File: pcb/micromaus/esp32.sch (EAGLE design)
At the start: 1 part, among them U1 ESP32-S2-WROOM

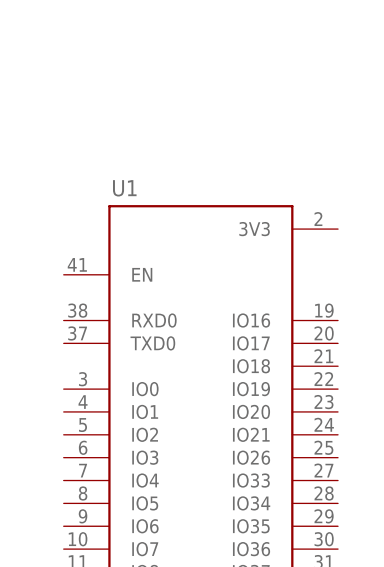
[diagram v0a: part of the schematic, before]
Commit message: added resistor
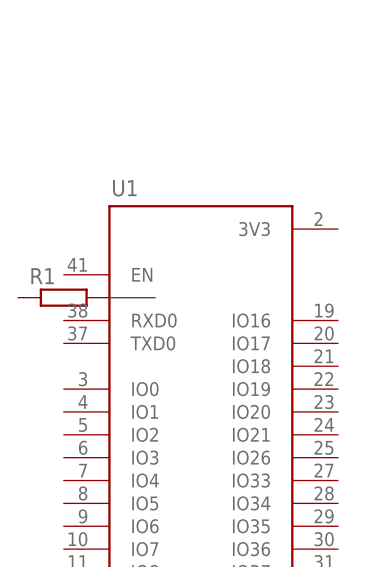
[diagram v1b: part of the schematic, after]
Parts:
- added R1: (no value), rcl:R-EU_R0603
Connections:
- new net N$1: R1.2, U1.IO0
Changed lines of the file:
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@@
 <drawing>
 <settings>
-<setting alwaysvectorfont="yes"/>
+<setting alwaysvectorfont="no"/>
 <setting verticaltext="up"/>
 </settings>
@@
 <layers>
 <layer number="1" name="Top" color="4" fill="1" visible="no" active="no"/>
+<layer number="2" name="Route2" color="1" fill="3" visible="no" active="no"/>
+<layer number="3" name="Route3" color="4" fill="3" visible="no" active="no"/>
+<layer number="4" name="Route4" color="1" fill="4" visible="no" active="no"/>
+<layer number="5" name="Route5" color="4" fill="4" visible="no" active="no"/>
+<layer number="6" name="Route6" color="1" fill="8" visible="no" active="no"/>
+<layer number="7" name="Route7" color="4" fill="8" visible="no" active="no"/>
+<layer number="8" name="Route8" color="1" fill="2" visible="no" active="no"/>
+<layer number="9" name="Route9" color="4" fill="2" visible="no" active="no"/>
+<layer number="10" name="Route10" color="1" fill="7" visible="no" active="no"/>
+<layer number="11" name="Route11" color="4" fill="7" visible="no" active="no"/>
+<layer number="12" name="Route12" color="1" fill="5" visible="no" active="no"/>
+<layer number="13" name="Route13" color="4" fill="5" visible="no" active="no"/>
+<layer number="14" name="Route14" color="1" fill="6" visible="no" active="no"/>
+<layer number="15" name="Route15" color="4" fill="6" visible="no" active="no"/>
 <layer number="16" name="Bottom" color="1" fill="1" visible="no" active="no"/>
 <layer number="17" name="Pads" color="2" fill="1" visible="no" active="no"/>
@@
 <parts>
 <part name="U1" library="ESP32-S2-WROOM" deviceset="ESP32-S2-WROOM" device=""/>
+<part name="R1" library="rcl" library_urn="urn:adsk.eagle:library:334" deviceset="R-EU_" device="R0603" package3d_urn="urn:adsk.eagle:package:23555/3"/>
 </parts>
 <sheets>
@@
 <attribute name="VALUE" x="58.3733" y="2.4319" size="1.78345" layer="96"/>
 </instance>
+<instance part="R1" gate="G$1" x="53.34" y="60.96" smashed="yes">
+<attribute name="NAME" x="49.53" y="62.4586" size="1.778" layer="95"/>
+<attribute name="VALUE" x="49.53" y="57.658" size="1.778" layer="96"/>
+</instance>
 </instances>
 <busses>
 </busses>
 <nets>
+<net name="N$1" class="0">
+<segment>
+<pinref part="R1" gate="G$1" pin="2"/>
+<pinref part="U1" gate="G$1" pin="IO0"/>
+<wire x1="58.42" y1="60.96" x2="63.5" y2="60.96" width="0.1524" layer="91"/>
+</segment>
+</net>
 </nets>
 </sheet>
@@
 </schematic>
 </drawing>
+<compatibility>
+<note version="8.2" severity="warning">
+Since Version 8.2, EAGLE supports online libraries. The ids
+of those online libraries will not be understood (or retained)
+with this version.
+</note>
+<note version="8.3" severity="warning">
+Since Version 8.3, EAGLE supports URNs for individual library
+assets (packages, symbols, and devices). The URNs of those assets
+will not be understood (or retained) with this version.
+</note>
+<note version="8.3" severity="warning">
+Since Version 8.3, EAGLE supports the association of 3D packages
+with devices in libraries, schematics, and board files. Those 3D
+packages will not be understood (or retained) with this version.
+</note>
+<note version="8.4" severity="warning">
+Since Version 8.4, EAGLE supports properties for SPICE simulation.
+Probes in schematics and SPICE mapping objects found in parts and library devices
+will not be understood with this version. Update EAGLE to the latest version
+for full support of SPICE simulation.
+</note>
+</compatibility>
 </eagle>

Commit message: added shit
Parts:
- added IC1: EPF10K30-Q240, altera:EPF10K30-Q240

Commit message: updated libs & wip usb uart
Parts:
- added IC2: CP2102, silabs:CP2102
- added U2: CH340C, CH340C:CH340C
- added X1: MINI-USB_SHIELD5P2-32005-601, con-cypressindustries:MINI-USB_SHIELD5P2-32005-601
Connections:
- new net GND: X1G41.4, X1G41.5
- new net N$3: U2.VCC
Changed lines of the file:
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@@
 <drawing>
 <settings>
-<setting alwaysvectorfont="no"/>
+<setting alwaysvectorfont="yes"/>
 <setting verticaltext="up"/>
 </settings>
@@
 <part name="R1" library="rcl" library_urn="urn:adsk.eagle:library:334" deviceset="R-EU_" device="R0603" package3d_urn="urn:adsk.eagle:package:23555/3"/>
 <part name="IC1" library="altera" library_urn="urn:adsk.eagle:library:97" deviceset="EPF10K30-Q240" device="" package3d_urn="urn:adsk.eagle:package:8081272/1"/>
+<part name="IC2" library="silabs" library_urn="urn:adsk.eagle:library:358" deviceset="CP210*" device="" package3d_urn="urn:adsk.eagle:package:26377/1" technology="2"/>
+<part name="U2" library="CH340C" deviceset="CH340C" device=""/>
+<part name="X1" library="con-cypressindustries" library_urn="urn:adsk.eagle:library:138" deviceset="MINI-USB_SHIELD5P2-" device="32005-601" package3d_urn="urn:adsk.eagle:package:6465/1"/>
+<part name="SUPPLY1" library="supply2" library_urn="urn:adsk.eagle:library:372" deviceset="GND" device=""/>
+<part name="C1" library="docu-dummy" library_urn="urn:adsk.eagle:library:215" deviceset="C" device=""/>
+<part name="C2" library="docu-dummy" library_urn="urn:adsk.eagle:library:215" deviceset="C" device=""/>
 </parts>
 <sheets>
@@
 </segment>
 </net>
+</nets>
+</sheet>
+<sheet>
+<description>USB-UART</description>
+<plain>
+</plain>
+<instances>
+<instance part="IC2" gate="G$1" x="101.6" y="17.78" smashed="yes">
+<attribute name="NAME" x="93.98" y="29.21" size="1.778" layer="95"/>
+<attribute name="VALUE" x="88.9" y="-2.54" size="1.778" layer="96"/>
+</instance>
+<instance part="U2" gate="G$1" x="99.06" y="73.66" smashed="yes" rot="MR0">
+<attribute name="NAME" x="109.22" y="94.615" size="1.778" layer="95" rot="MR0"/>
+<attribute name="VALUE" x="109.22" y="53.34" size="1.778" layer="96" rot="MR0"/>
+</instance>
+<instance part="X1" gate="G41" x="15.24" y="53.34" smashed="yes" rot="R180">
+<attribute name="NAME" x="17.78" y="41.91" size="1.778" layer="95" rot="R180"/>
+<attribute name="VALUE" x="5.08" y="60.96" size="1.778" layer="96" rot="R270"/>
+</instance>
+<instance part="SUPPLY1" gate="GND" x="45.72" y="48.26" smashed="yes">
+<attribute name="VALUE" x="43.815" y="45.085" size="1.778" layer="96"/>
+</instance>
+<instance part="C1" gate="G$1" x="88.9" y="111.76" smashed="yes"/>
+<instance part="C2" gate="G$1" x="99.06" y="111.76" smashed="yes"/>
+</instances>
+<busses>
+</busses>
+<nets>
+<net name="GND" class="0">
+<segment>
+<pinref part="X1" gate="G41" pin="5"/>
+<wire x1="20.32" y1="58.42" x2="45.72" y2="58.42" width="0.1524" layer="91"/>
+<wire x1="45.72" y1="58.42" x2="45.72" y2="55.88" width="0.1524" layer="91"/>
+<pinref part="X1" gate="G41" pin="4"/>
+<wire x1="20.32" y1="55.88" x2="45.72" y2="55.88" width="0.1524" layer="91"/>
+<wire x1="45.72" y1="55.88" x2="45.72" y2="50.8" width="0.1524" layer="91"/>
+<junction x="45.72" y="55.88"/>
+<pinref part="SUPPLY1" gate="GND" pin="GND"/>
+</segment>
+</net>
+<net name="N$3" class="0">
+<segment>
+<pinref part="U2" gate="G$1" pin="VCC"/>
+<wire x1="83.82" y1="91.44" x2="78.74" y2="91.44" width="0.1524" layer="91"/>
+<wire x1="78.74" y1="91.44" x2="78.74" y2="114.3" width="0.1524" layer="91"/>
+<wire x1="78.74" y1="114.3" x2="109.22" y2="114.3" width="0.1524" layer="91"/>
+<wire x1="109.22" y1="114.3" x2="109.22" y2="121.92" width="0.1524" layer="91"/>
+</segment>
+</net>

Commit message: feat: add usb-uart schematics
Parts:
- removed IC2: CP2102, silabs:CP2102
- removed U2: CH340C, CH340C:CH340C
- removed X1: MINI-USB_SHIELD5P2-32005-601, con-cypressindustries:MINI-USB_SHIELD5P2-32005-601
- added C1: 4.7uF, rcl:C-EUC0805
- added C2: 100nF, rcl:C-EUC0805
- added D1: SP0503BAHTG, SP0503BAHTG:SP0503BAHTG
- added U$1: MICRO-USBV2, microusb:MICRO-USBV2
- added U$2: 1N5819, 1N5819:1N5819
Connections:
- removed net GND: X1G41.4, X1G41.5
- removed net N$3: U2.VCC
- new net 0: C1.2, C2.2, U$1.GND
- new net D+: U$1.D+
- new net D-: D1.3, U$1.D-
- new net N$4: C1.1, C2.1, D1.2, D1.4, U$1.VCC, U$2.A
- new net N$6: D1.1
